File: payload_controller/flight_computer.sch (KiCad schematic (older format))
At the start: 0 parts

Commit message: Continuing layout
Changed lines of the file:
@@
 F9 "SDA" I L 9100 4000 50
 F10 "SCL" I L 9100 3900 50
+F11 "ALERT" I L 9100 4100 50
 $EndSheet
 $Sheet
@@
 F19 "ADC_SYNC" I R 7650 5650 50
 F20 "REVERSE_BIAS" I R 7650 3550 50
+F21 "ALERT" O R 7650 4100 50
 $EndSheet
 $Sheet
@@
 Wire Wire Line
 	8150 4000 9100 4000
+Wire Wire Line
+	7650 4100 9100 4100
 $EndSCHEMATC

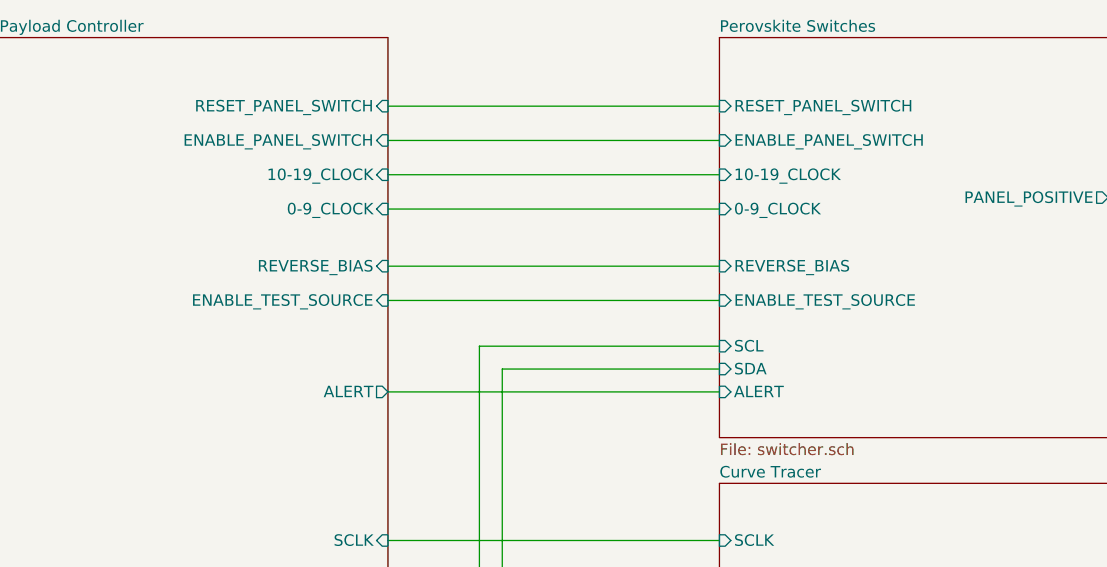
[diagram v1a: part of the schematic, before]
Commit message: Completed routing
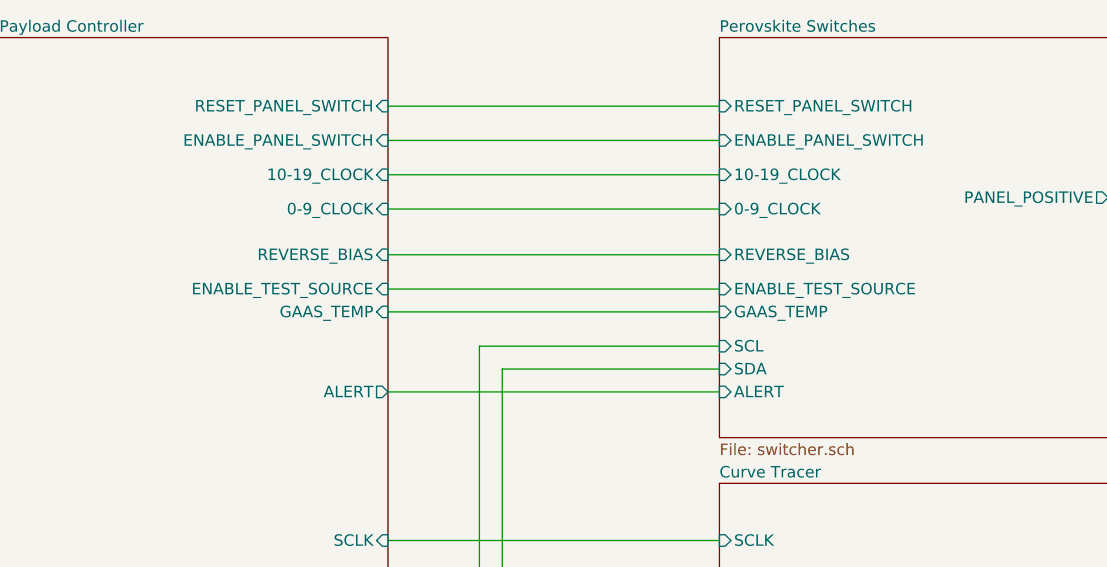
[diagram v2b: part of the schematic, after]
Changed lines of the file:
@@
 F0 "Perovskite Switches" 50
 F1 "switcher.sch" 50
-F2 "ENABLE_TEST_SOURCE" I L 9100 3700 50
+F2 "ENABLE_TEST_SOURCE" I L 9100 3650 50
 F3 "RESET_PANEL_SWITCH" I L 9100 2850 50
 F4 "ENABLE_PANEL_SWITCH" I L 9100 3000 50
@@
 F6 "0-9_CLOCK" I L 9100 3300 50
 F7 "PANEL_POSITIVE" O R 10800 3250 50
-F8 "REVERSE_BIAS" I L 9100 3550 50
+F8 "REVERSE_BIAS" I L 9100 3500 50
 F9 "SDA" I L 9100 4000 50
 F10 "SCL" I L 9100 3900 50
 F11 "ALERT" I L 9100 4100 50
+F12 "GAAS_TEMP" I L 9100 3750 50
 $EndSheet
 $Sheet
@@
 F4 "10-19_CLOCK" I R 7650 3150 50
 F5 "0-9_CLOCK" I R 7650 3300 50
-F6 "ENABLE_TEST_SOURCE" I R 7650 3700 50
+F6 "ENABLE_TEST_SOURCE" I R 7650 3650 50
 F7 "SCL" I R 7650 7100 50
 F8 "SDA" I R 7650 7200 50
@@
 F18 "ADC_DRDY" I R 7650 5500 50
 F19 "ADC_SYNC" I R 7650 5650 50
-F20 "REVERSE_BIAS" I R 7650 3550 50
+F20 "REVERSE_BIAS" I R 7650 3500 50
 F21 "ALERT" O R 7650 4100 50
+F22 "GAAS_TEMP" I R 7650 3750 50
 $EndSheet
 $Sheet
@@
 	7650 3300 9100 3300
 Wire Wire Line
-	7650 3550 9100 3550
+	7650 3500 9100 3500
 Wire Wire Line
-	7650 3700 9100 3700
+	7650 3650 9100 3650
 Wire Wire Line
 	7650 4750 9100 4750
@@
 Wire Wire Line
 	7650 4100 9100 4100
+Wire Wire Line
+	7650 3750 9100 3750
 $EndSCHEMATC
